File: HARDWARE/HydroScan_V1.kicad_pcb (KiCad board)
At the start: 4 copper layers, 202 x 100 mm, 124 parts, among them CN3 DB128V-5.08-2P-GN-S, Q1 AO4435_C2944310, Q13 2n3904S-RTK/PS_C18536, Q14 2n3904S-RTK/PS_C18536, Q15 2n3904S-RTK/PS_C18536, Q16 2n3904S-RTK/PS_C18536, SW2 BOOT, SW4 RESET, U1 IP2312-4V35, U10 DB125-3.81-2P-BK-S, U11 DB125-3.81-2P-BK-S, U13 ESP32-WROOM-32D, U14 CH340C, U15 CH340C, U16 ESP32-WROOM-32D, U2 BQ25798RQMR, U2 L298N, U3 CH224K, U4 CN3795, U7 LM2576HVS-3.3, U8 DB125-3.81-2P-BK-S, U9 DB125-3.81-2P-BK-S

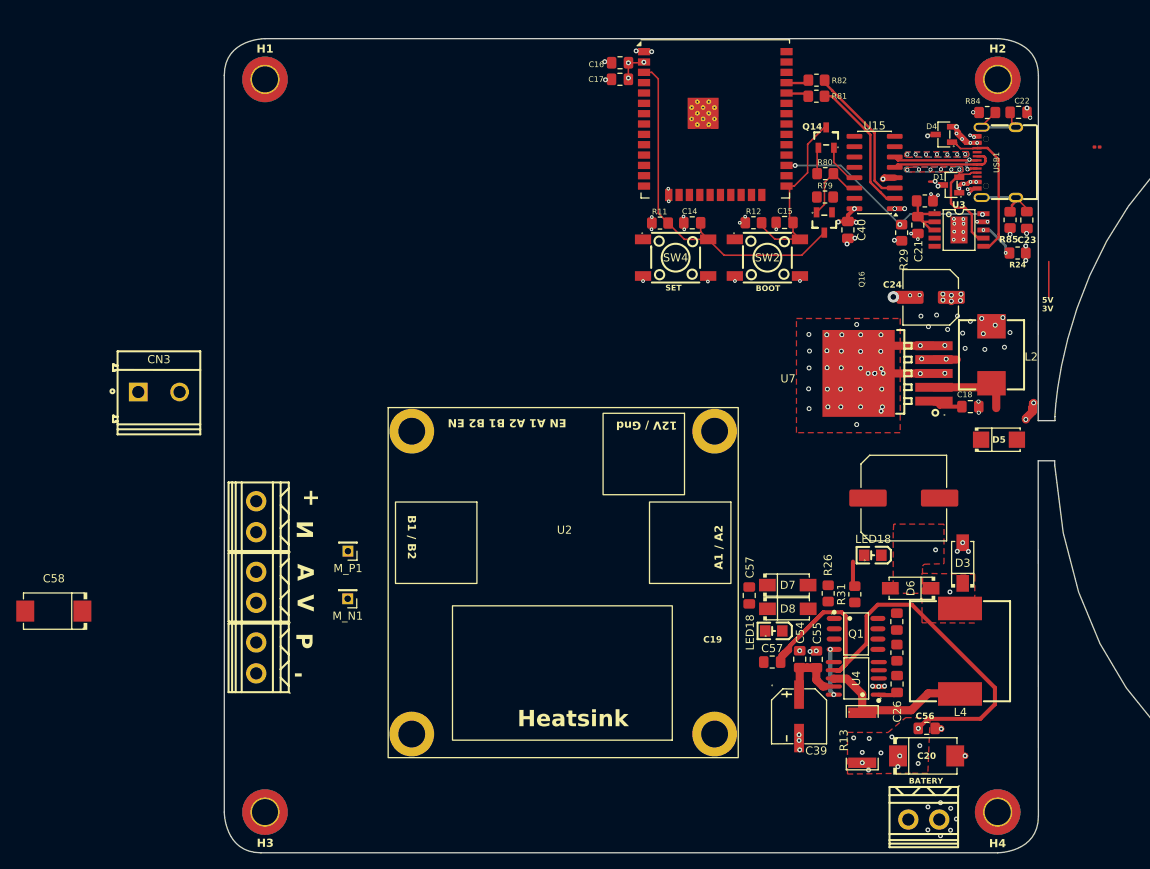
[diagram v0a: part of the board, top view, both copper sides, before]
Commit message: powering rooting finish
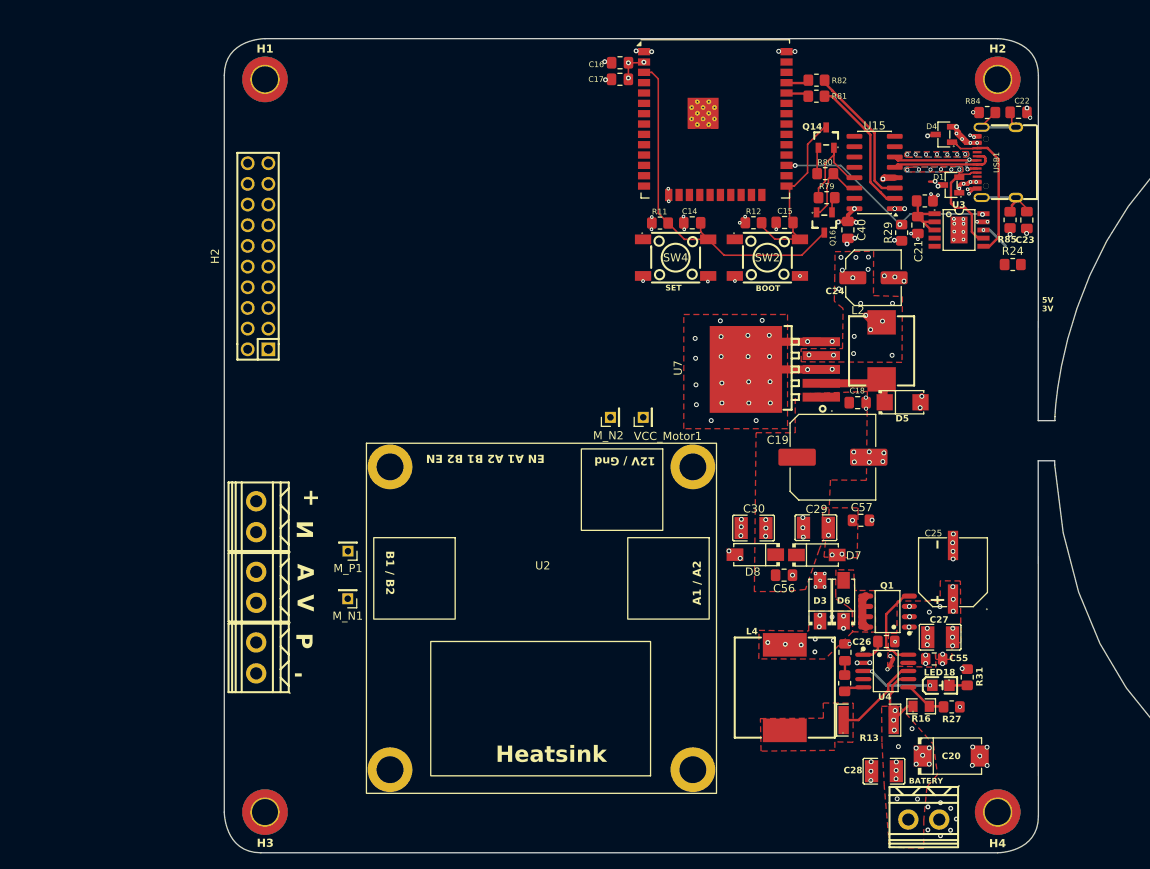
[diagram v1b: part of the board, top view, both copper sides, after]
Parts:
- removed C32: 0.1uf, Capacitor_SMD:C_0201_0603Metric
- removed C39: RVT1V101M0607, EasyEDA:CAP-SMD_BD6.3-L6.6-W6.6-LS7.6-FD
- removed C54: 10uF, Capacitor_SMD:C_0805_2012Metric_Pad1.18x1.45mm_HandSolder
- removed the C57 at (147.3, 196.6)
- removed the C57 at (144.5, 188.4)
- removed C58: CA45-D035K226T, EasyEDA:CAP-SMD_L7.3-W4.3-R-RD
- removed CN3: DB128V-5.08-2P-GN-S, EasyEDA:CONN-TH_2P-P5.08_DIBO_DB128V-5.08
- removed the LED18 at (147.5, 192.8)
- removed the LED18 at (159.7, 183.4)
- removed R26: 2.2k, Resistor_SMD:R_0805_2012Metric_Pad1.20x1.40mm_HandSolder
- added C25: RVT1V221M0810, EasyEDA:CAP-SMD_BD8.0-L8.3-W8.3-LS9.1-FD, F.Cu at (169.5, 185.5)
- added C27: CL32B106KBJNNNE, EasyEDA:C1210, F.Cu at (167.9, 193.5)
- added C28: CL32B106KBJNNNE, EasyEDA:C1210, F.Cu at (161.0, 210.0)
- added C29: CL32B106KBJNNNE, EasyEDA:C1210, F.Cu at (152.7, 180.1)
- added C30: CL32B106KBJNNNE, EasyEDA:C1210, F.Cu at (145.0, 180.1)
- added C57: 0.1uf, Capacitor_SMD:C_0805_2012Metric_Pad1.18x1.45mm_HandSolder, F.Cu at (158.2, 179.2)
- added H2: 2.54-2*10, EasyEDA:HDR-TH_20P-P2.54-V-M-R2-C10-S2.54, F.Cu at (84.1, 146.7)
- added LED18: YLED0805G, EasyEDA:LED0805-FD-GREEN, F.Cu at (168.0, 199.4)
- added M_N2: M_GND, Connector_PinHeader_2.00mm:PinHeader_1x01_P2.00mm_Vertical, F.Cu at (127.4, 166.5)
- added NT1: NetTie_2, NetTie:NetTie-2_SMD_Pad0.5mm, F.Cu at (161.9, 196.6)
- added R16: RC0805FR-07390KL, EasyEDA:R0805, F.Cu at (165.6, 202.0)
- added R27: 41.2K, Resistor_SMD:R_0805_2012Metric_Pad1.20x1.40mm_HandSolder, F.Cu at (169.3, 202.1)
- added VCC_Motor1: M_VCC, Connector_PinHeader_2.00mm:PinHeader_1x01_P2.00mm_Vertical, F.Cu at (131.5, 166.5)
- C56: value 10uF -> 0.1uf
- moved C56 25.7 mm to (148.8, 185.9)
- moved L4 22.0 mm to (148.8, 199.7)
- moved D3 18.1 mm to (153.2, 189.0)
- moved R31 17.2 mm to (171.3, 198.4), turned to -90 degrees
- moved C55 14.5 mm to (167.2, 196.2), turned to 180 degrees
- moved U7 13.8 mm to (148.7, 160.6)
- moved C18 13.8 mm to (157.8, 164.7)
- moved L2 13.5 mm to (160.7, 158.3)
- moved D5 12.7 mm to (163.3, 164.7)
- moved C19 10.1 mm to (154.8, 171.4)
- moved D6 8.38 mm to (156.1, 189.0), turned to 90 degrees
- moved D8 7.76 mm to (145.2, 183.4), turned to 180 degrees
- moved R25 7.43 mm to (156.2, 199.2)
- moved C24 7.43 mm to (159.7, 149.4), turned to 0 degrees
- moved C53 7.41 mm to (156.2, 195.4)
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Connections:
- net /CSP renamed Net-(U4-CSP)
- net /DRAIN renamed Net-(D6-A)
- C20 pad 1: /1 -> /VCC_MOTOR
- C53 pad 1: GND -> GND2
- C56 pad 2: /1 -> /VCC_REG
- D8 pad 1: /1 -> /VCC_MOTOR
- R13 pad 2: /1 -> /VCC_MOTOR
- U11 pad 2: /V_BATTERY__1 -> /VCC_MOTOR
- U4 pad 2: GND -> GND2
- U4 pad 7: /1 -> /VCC_MOTOR
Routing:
- net /1: track 69.8 -> 0.00 mm, vias 12 -> 0
- net 3.3V: track 28.6 -> 47.0 mm, vias 24 -> 29
- net /VCC_MOTOR: track 0.00 -> 11.5 mm, vias 0 -> 20
- net /CHARG: track 0.00 -> 9.27 mm, vias 0 -> 2
- net Net-(U4-CSP): track 18.8 -> 10.9 mm
- net GND: track 71.7 -> 79.0 mm, vias 124 -> 132
- net /DTR_1: track 5.11 -> 12.0 mm
- net Net-(U4-FB): track 0.00 -> 5.34 mm
- net /V5_1: track 31.3 -> 26.4 mm, vias 20 -> 31
- net Net-(Q1-G): track 6.24 -> 10.9 mm, vias 2 -> 0
- net Net-(D6-A): track 0.00 -> 4.15 mm, vias 1 -> 0
- net /VCC_REG: track 3.81 -> 0.10 mm
- net Net-(U4-COM): track 0.00 -> 2.50 mm
- net Net-(Q16-B): track 0.00 -> 1.94 mm
- net Net-(C53-Pad2): track 0.00 -> 1.77 mm
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- added copper zone on F.Cu, net /V5_1
- added copper zone on F.Cu, net /VCC_MOTOR
- added copper zone on In2.Cu, net /VCC_MOTOR
- added copper zone on F.Cu, net /VCC_REG
- added copper zone on F.Cu, net 3.3V
- added copper zone on In1.Cu, net GND2
- added copper zone on F.Cu, net Net-(U4-CSP)
- removed copper zone on F.Cu, net /1
- removed copper zone on In2.Cu, net /V_BATTERY__1

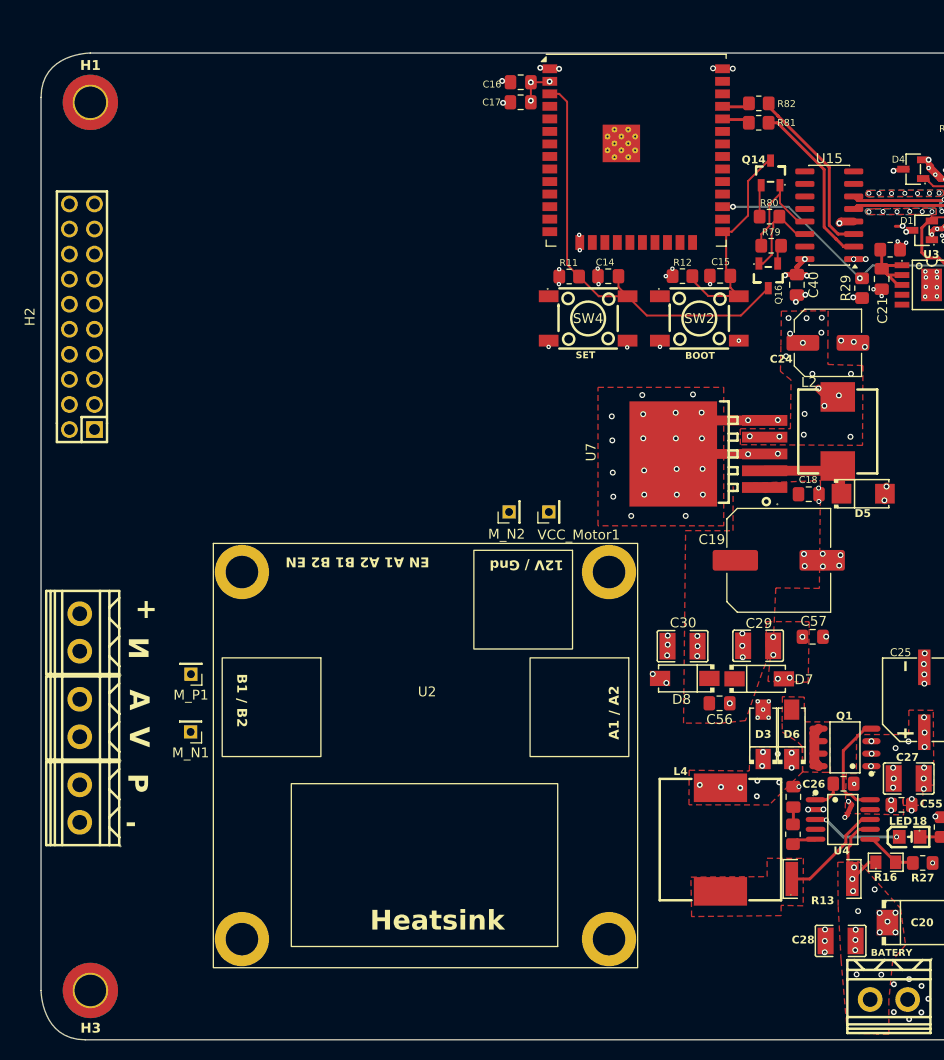
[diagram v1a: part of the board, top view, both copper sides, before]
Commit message: Update of design the power
update of charging
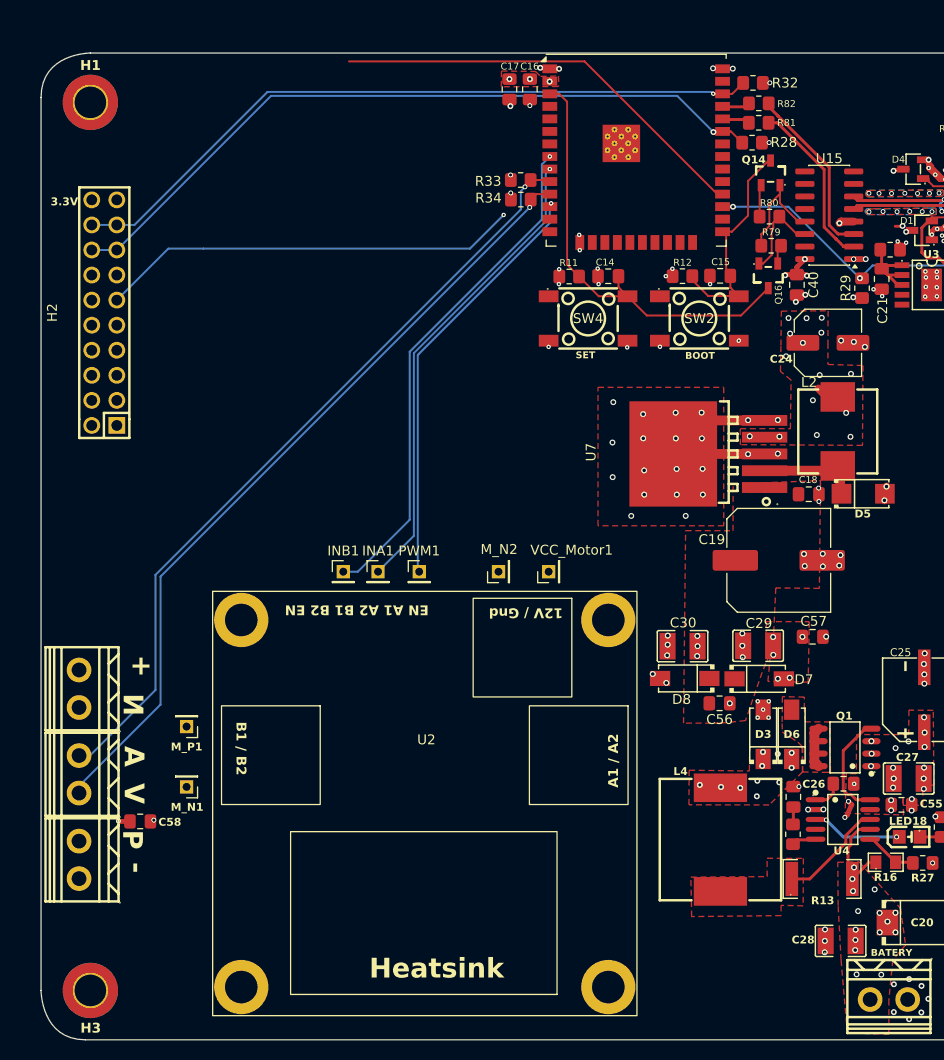
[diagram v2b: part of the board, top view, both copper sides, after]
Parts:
- added C58: 0.1uf, Capacitor_SMD:C_0805_2012Metric_Pad1.18x1.45mm_HandSolder, F.Cu at (90.0, 197.9)
- added INA1: INA, Connector_PinHeader_2.00mm:PinHeader_1x01_P2.00mm_Vertical, F.Cu at (114.2, 172.6)
- added INB1: INB, Connector_PinHeader_2.00mm:PinHeader_1x01_P2.00mm_Vertical, F.Cu at (110.6, 172.6)
- added PWM1: PWM_1, Connector_PinHeader_2.00mm:PinHeader_1x01_P2.00mm_Vertical, F.Cu at (118.3, 172.6)
- added R28: 4.7K, Resistor_SMD:R_0805_2012Metric_Pad1.20x1.40mm_HandSolder, F.Cu at (152.1, 129.1)
- added R32: 4.7K, Resistor_SMD:R_0805_2012Metric_Pad1.20x1.40mm_HandSolder, F.Cu at (152.2, 123.0)
- added R33: 4.7K, Resistor_SMD:R_0805_2012Metric_Pad1.20x1.40mm_HandSolder, F.Cu at (128.6, 132.9)
- added R34: 4.7K, Resistor_SMD:R_0805_2012Metric_Pad1.20x1.40mm_HandSolder, F.Cu at (128.6, 134.8)
- moved M_N2 6.14 mm to (126.4, 172.6)
- moved VCC_Motor1 6.05 mm to (131.4, 172.6)
- moved U10 5.70 mm to (83.9, 184.4)
- moved U8 5.70 mm to (83.9, 201.8)
- moved U9 5.70 mm to (83.9, 193.1)
- moved M_N1 5.59 mm to (94.8, 194.4)
- moved M_P1 5.33 mm to (94.8, 188.3)
- moved U2 4.86 mm to (119.4, 171.6)
- moved H2 2.30 mm to (86.4, 146.3)
- moved C17 1.73 mm to (127.5, 123.7), turned to -90 degrees
- moved C16 1.17 mm to (129.5, 123.7), turned to -90 degrees
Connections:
- H2 pad 11: unconnected-(H2-Pad11) -> /IO27_1
- H2 pad 12: unconnected-(H2-Pad12) -> /IO17_1
- H2 pad 14: unconnected-(H2-Pad14) -> /IO16_1
- H2 pad 15: unconnected-(H2-Pad15) -> /IO21_1
- H2 pad 16: unconnected-(H2-Pad16) -> /IO21_1
- H2 pad 17: unconnected-(H2-Pad17) -> /IO22_1
- H2 pad 18: unconnected-(H2-Pad18) -> /IO22_1
- H2 pad 19: unconnected-(H2-Pad19) -> 3.3V
- H2 pad 20: unconnected-(H2-Pad20) -> 3.3V
- U9 pad 1: unconnected-(U9-Pad1) -> /IO26_1
- U9 pad 2: unconnected-(U9-Pad2) -> /IO25_1
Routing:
- net /IO27_1: track 0.00 -> 86.2 mm, vias 0 -> 2
- net /IO26_1: track 0.00 -> 81.3 mm, vias 0 -> 1
- net /IO25_1: track 0.00 -> 79.9 mm, vias 0 -> 1
- net /IO21_1: track 0.00 -> 74.4 mm, vias 0 -> 1
- net /IO22_1: track 0.00 -> 72.1 mm, vias 0 -> 1
- net /IO32_1: track 0.00 -> 51.7 mm, vias 0 -> 1
- net /IO33_1: track 0.00 -> 48.0 mm, vias 0 -> 1
- net /IO17_1: track 0.00 -> 43.4 mm
- net 3.3V: track 47.0 -> 22.8 mm, vias 29 -> 32
- net GND: track 79.0 -> 78.8 mm, vias 132 -> 130
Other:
- board text added: "3.3V"

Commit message: latest updates
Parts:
- removed BOOT1: BOOT, EasyEDA:SW-SMD_4P-L6.0-W6.0-P4.50-LS8.2
- removed C1, C4, C6: 10uf_25v, Capacitor_SMD:C_0805_2012Metric_Pad1.18x1.45mm_HandSolder
- removed C10, C12, C13: 22uf, Capacitor_SMD:C_0805_2012Metric_Pad1.18x1.45mm_HandSolder
- removed C11, C9: 10uf, Capacitor_SMD:C_0805_2012Metric_Pad1.18x1.45mm_HandSolder
- removed C2, C3: 0.1uf_50v, Capacitor_SMD:C_0805_2012Metric_Pad1.18x1.45mm_HandSolder
- removed C5: 100nf, Capacitor_SMD:C_0805_2012Metric_Pad1.18x1.45mm_HandSolder
- removed C7, C8: 0.1uf, Capacitor_SMD:C_0805_2012Metric_Pad1.18x1.45mm_HandSolder
- removed D22: 1N5819HW-7-F, EasyEDA:SOD-123_L2.7-W1.6-LS3.7-RD
- removed D27, D28, D29, D30, D31: LESD5D5.0CT1G, EasyEDA:SOD-523_L1.2-W0.8-LS1.6-BI
- removed INA1: INA, Connector_PinHeader_2.00mm:PinHeader_1x01_P2.00mm_Vertical
- removed L1: APH0420T1R0M, EasyEDA:IND-SMD_L4.4-W4.2
- removed LED10, LED11, LED16, LED18, LED9: YLED0805G, EasyEDA:LED0805-FD-GREEN
- removed Q13, Q15: 2n3904S-RTK/PS_C18536, EasyEDA:SOT-23-3_L2.9-W1.3-P1.90-LS2.4-TR
- removed R1: 2R, Resistor_SMD:R_0805_2012Metric_Pad1.20x1.40mm_HandSolder
- removed R10: 0.5R, Resistor_SMD:R_0805_2012Metric_Pad1.20x1.40mm_HandSolder
- removed R18, R6: 2.2k, Resistor_SMD:R_0805_2012Metric_Pad1.20x1.40mm_HandSolder
- removed R2: 51k, Resistor_SMD:R_0805_2012Metric_Pad1.20x1.40mm_HandSolder
- removed R3, R4: 100, Resistor_SMD:R_0805_2012Metric_Pad1.20x1.40mm_HandSolder
- removed R74, R75, R9: 1k, Resistor_SMD:R_0805_2012Metric_Pad1.20x1.40mm_HandSolder
- removed RESET1: RESET, EasyEDA:SW-SMD_4P-L6.0-W6.0-P4.50-LS8.2
- removed SGM2212-3.1: ~, Package_TO_SOT_SMD:SOT-223
- removed U1: IP2312-4V35, EasyEDA:ESOP-8_L4.9-W3.9-P1.27-LS6.0-BL-EP
- removed U14: CH340C, Package_SO:SOIC-16_3.9x9.9mm_P1.27mm
- removed the U2 at (304.9, 134.9)
- removed USB2: HX-TYPE-C 16P 180 LT H15.0, EasyEDA:USB-C-SMD_HX-TYPE-C-16P-180-LT-H15.0
- added C31: 100nf, Capacitor_SMD:C_0805_2012Metric_Pad1.18x1.45mm_HandSolder, F.Cu at (163.3, 143.8)
- added C59: 0.1uf, Capacitor_SMD:C_0805_2012Metric_Pad1.18x1.45mm_HandSolder, F.Cu at (128.6, 126.6)
- added C60: 0.1uf, Capacitor_SMD:C_0805_2012Metric_Pad1.18x1.45mm_HandSolder, F.Cu at (128.6, 128.6)
- added G***: LOGO, imagen1:13, F.Cu at (113.3, 145.6)
- added INB1: INB1, Connector_PinHeader_2.00mm:PinHeader_1x01_P2.00mm_Vertical, F.Cu at (111.6, 172.3)
- added R26: 10k, Resistor_SMD:R_0805_2012Metric_Pad1.20x1.40mm_HandSolder, F.Cu at (158.8, 202.1)
- added R30: 100K, Resistor_SMD:R_0805_2012Metric_Pad1.20x1.40mm_HandSolder, F.Cu at (162.6, 201.9)
- added R35: 10k, Resistor_SMD:R_0805_2012Metric_Pad1.20x1.40mm_HandSolder, F.Cu at (124.4, 163.4)
- added R36: 30k, Resistor_SMD:R_0805_2012Metric_Pad1.20x1.40mm_HandSolder, F.Cu at (122.4, 163.4)
- added THECPCENTER: LOGO, images:IMG1, F.Cu at (119.8, 211.9)
- added U5: LM358DR, EasyEDA:SOIC-8_L5.0-W4.0-P1.27-LS6.0-BL, F.Cu at (128.3, 163.6)
- GND1: renamed from M_N2; value M_GND -> PH_GND
- INB2: renamed from INB1; value INB -> INB2
- PWM1: value PWM_1 -> PWM
- R31: value 2.2k -> 10k
- moved R22 149.0 mm to (169.5, 152.2)
- moved R14 147.3 mm to (169.2, 162.1)
- moved R17 146.9 mm to (169.2, 167.1)
- moved R15 144.5 mm to (169.3, 157.2)
- moved 3.3V1 119.5 mm to (173.3, 162.1)
- moved BAT1 118.8 mm to (173.3, 167.1)
- moved RUN1 116.2 mm to (173.3, 157.1)
- moved USB3 111.5 mm to (173.3, 152.2)
- moved R31 68.4 mm to (151.1, 133.0), turned to 90 degrees
- moved PWM1 13.4 mm to (104.9, 172.3)
- moved C58 11.0 mm to (84.5, 207.4), turned to 0 degrees
- moved R24 6.58 mm to (170.3, 147.1)
- moved L4 6.33 mm to (148.7, 206.0)
- moved D3 5.32 mm to (150.3, 193.5)
- moved D6 5.24 mm to (153.4, 193.5)
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- renumbered LED12 to 3.3V1, LED15 to BAT1, LED13 to RUN1, LED17 to USB3, VCC_Motor1 to VCC1
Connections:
- H2 pad 10: unconnected-(H2-Pad10) -> GND
- H2 pad 11: /IO27_1 -> /IO18_1
- H2 pad 12: /IO17_1 -> GND
- H2 pad 13: unconnected-(H2-Pad13) -> /IO21_1
- H2 pad 14: /IO16_1 -> /IO21_1
- H2 pad 15: /IO21_1 -> /IO22_1
- H2 pad 16: /IO21_1 -> /IO22_1
- H2 pad 17: /IO22_1 -> /IO23_1
- H2 pad 18: /IO22_1 -> /IO13_1
- H2 pad 5: unconnected-(H2-Pad5) -> 3.3V
- H2 pad 6: unconnected-(H2-Pad6) -> 3.3V
- H2 pad 7: unconnected-(H2-Pad7) -> /IO32_1
- H2 pad 8: unconnected-(H2-Pad8) -> GND
- H2 pad 9: unconnected-(H2-Pad9) -> /VP_1
- INB2 pad 1: /IO32_1 -> /IO27_1
- PWM1 pad 1: /IO27_1 -> /IO26_1
- R17 pad 1: unconnected-(R17-Pad1) -> /VCC_MOTOR
- R31 pad 1: /V5_1 -> /IO17_1
- R31 pad 2: Net-(LED18-A) -> 3.3V
- R33 pad 2: /IO25_1 -> /IO33_1
- R34 pad 2: /IO26_1 -> /IO25_1
- RUN1 pad 2: unconnected-(LED13-K-Pad2) -> /IO19_1
- U16 pad 14: /IO12_1 -> unconnected-(U16-IO12-Pad14)
- U16 pad 23: /IO15_1 -> unconnected-(U16-IO15-Pad23)
- U16 pad 24: /IO2_1 -> unconnected-(U16-IO2-Pad24)
- U16 pad 26: /IO4_1 -> unconnected-(U16-IO4-Pad26)
- U4 pad 3: /CHARG -> /IO17_1
- U9 pad 1: /IO26_1 -> /IO25_1
- U9 pad 2: /IO25_1 -> /IO33_1
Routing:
- net /IO18_1: track 0.00 -> 74.1 mm, vias 0 -> 1
- net /IO23_1: track 0.00 -> 67.4 mm, vias 0 -> 1
- net /IO13_1: track 0.00 -> 57.6 mm, vias 0 -> 2
- net /VP_1: track 0.00 -> 56.2 mm, vias 0 -> 1
- net /VCC_MOTOR: track 11.5 -> 67.3 mm, vias 20 -> 22
- net /IO17_1: track 43.4 -> 97.0 mm, vias 0 -> 2
- net /IO14_1: track 0.00 -> 44.2 mm, vias 0 -> 1
- net /IO19_1: track 0.00 -> 41.3 mm, vias 0 -> 2
- net /VN_1: track 0.00 -> 40.3 mm
- net /IO27_1: track 86.2 -> 46.9 mm, vias 2 -> 1
- net /IO33_1: track 48.0 -> 81.2 mm
- net /IO26_1: track 81.3 -> 49.3 mm
- net 3.3V: track 22.8 -> 42.0 mm, vias 32 -> 30
- net /CHARG: track 9.27 -> 0.00 mm, vias 2 -> 0
- net GND: track 78.8 -> 87.8 mm, vias 130 -> 139
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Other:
- board text added: "ALBERTO MÉNDEZ 2023-1969"
- board text added: "Automatizando la asistencia respiratoria para brindar una segunda oportunidad cuando cada segundo cuenta."
- board text added: "GND"
- board text added: "IO13"
- board text added: "IO18"
- board text added: "IO21"
- board text added: "IO22"
- board text added: "IO23"
- board text added: "IO32"
- board text added: "ISAÍAS MATOS 2024-0688"
- board text added: "MIGUEL RAMÍREZ 2024-1264"
- board text added: "PAUL MARTINEZ 2024-1267"
- board text added: "VP"
- board text removed: "3V"
- board text removed: "5V"
